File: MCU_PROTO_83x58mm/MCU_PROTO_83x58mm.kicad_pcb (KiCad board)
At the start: 2 copper layers, 75 x 49 mm, 251 parts, among them J1 Screw_Terminal_01x03, J10 Conn_01x01_Male, J2 Screw_Terminal_01x03, J3 Conn_01x20_Female, J4 Conn_01x20_Female, J5 Conn_01x20_Female, J6 Conn_01x20_Female, J7 Conn_01x20_Female, J8 Conn_01x20_Female, J9 Conn_01x01_Male

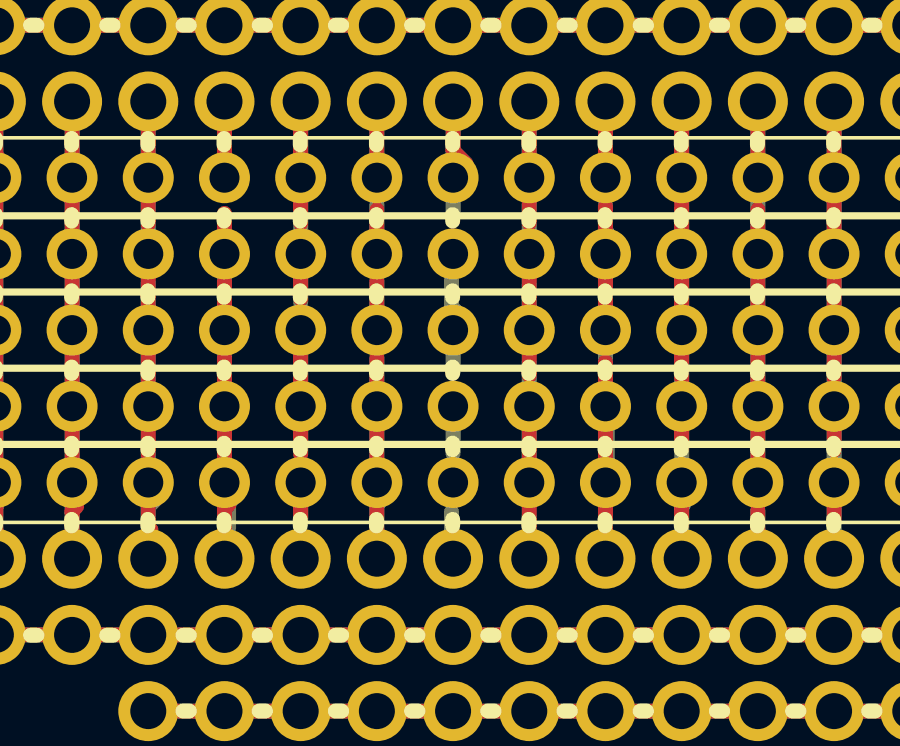
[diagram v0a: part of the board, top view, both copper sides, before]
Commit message: added missing trace
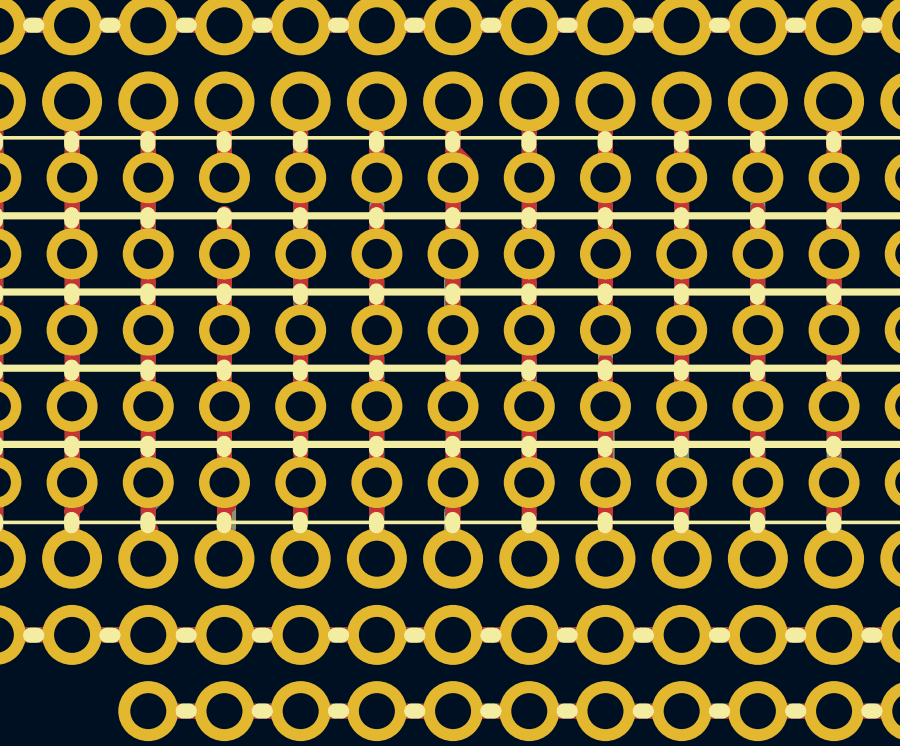
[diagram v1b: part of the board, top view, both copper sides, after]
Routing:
- net Net-(J8-Pad9): track 0.00 -> 4.41 mm
- net Net-(J7-Pad9): track 1.57 -> 4.44 mm
- net Net-(J6-Pad9): track 2.48 -> 4.79 mm
- net Net-(J5-Pad9): track 0.00 -> 2.21 mm
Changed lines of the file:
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@@
     (thickness 1.6)
     (drawings 284)
-    (tracks 720)
+    (tracks 728)
     (zones 0)
     (modules 251)
@@
   (segment (start 132.12 125.77) (end 132.12 124.1063) (width 0.5) (layer B.Cu) (net 74))
   (segment (start 132.12 125.77) (end 132.12 127.4718) (width 0.5) (layer F.Cu) (net 74))
+  (segment (start 129.58 125.77) (end 129.58 123.5564) (width 0.5) (layer F.Cu) (net 75))
   (segment (start 157.52 128.31) (end 157.52 126.7314) (width 0.5) (layer B.Cu) (net 76))
   (segment (start 157.52 128.31) (end 157.52 126.9092) (width 0.5) (layer F.Cu) (net 76))
@@
   (segment (start 129.5273 126.6317) (end 129.5273 127.5334) (width 0.5) (layer B.Cu) (net 87))
   (segment (start 129.58 128.31) (end 129.58 129.707) (width 0.5) (layer B.Cu) (net 87))
+  (segment (start 129.58 128.31) (end 129.58 125.9986) (width 0.5) (layer F.Cu) (net 87))
   (segment (start 157.52 130.85) (end 157.52 129.1444) (width 0.5) (layer B.Cu) (net 88))
   (segment (start 157.52 130.85) (end 157.52 128.7253) (width 0.5) (layer F.Cu) (net 88))
@@
   (segment (start 132.12 130.85) (end 132.12 132.6661) (width 0.5) (layer F.Cu) (net 98))
   (segment (start 129.58 130.85) (end 129.58 132.4248) (width 0.5) (layer B.Cu) (net 99))
+  (segment (start 129.58 130.85) (end 129.58 128.4751) (width 0.5) (layer F.Cu) (net 99))
+  (segment (start 129.58 128.4751) (end 129.3749 128.27) (width 0.5) (layer F.Cu) (net 99))
+  (segment (start 129.3749 126.3142) (end 129.5146 126.1745) (width 0.5) (layer F.Cu) (net 99))
   (segment (start 127.04 130.85) (end 127.04 129.3095) (width 0.5) (layer B.Cu) (net 100))
   (segment (start 127.04 130.85) (end 127.04 129.2117) (width 0.5) (layer F.Cu) (net 100))
@@
   (segment (start 132.12 133.39) (end 132.12 131.6463) (width 0.5) (layer B.Cu) (net 118))
   (segment (start 132.12 133.39) (end 132.12 134.9013) (width 0.5) (layer F.Cu) (net 118))
+  (segment (start 129.58 133.7202) (end 129.5146 133.6548) (width 0.5) (layer F.Cu) (net 119))
+  (segment (start 129.58 135.93) (end 129.58 133.7202) (width 0.5) (layer F.Cu) (net 119))
+  (segment (start 129.58 133.39) (end 129.58 131.278) (width 0.5) (layer F.Cu) (net 119))
   (segment (start 127.04 134.1355) (end 127.1143 134.0612) (width 0.5) (layer B.Cu) (net 120))
   (segment (start 127.04 135.93) (end 127.04 134.1355) (width 0.5) (layer B.Cu) (net 120))

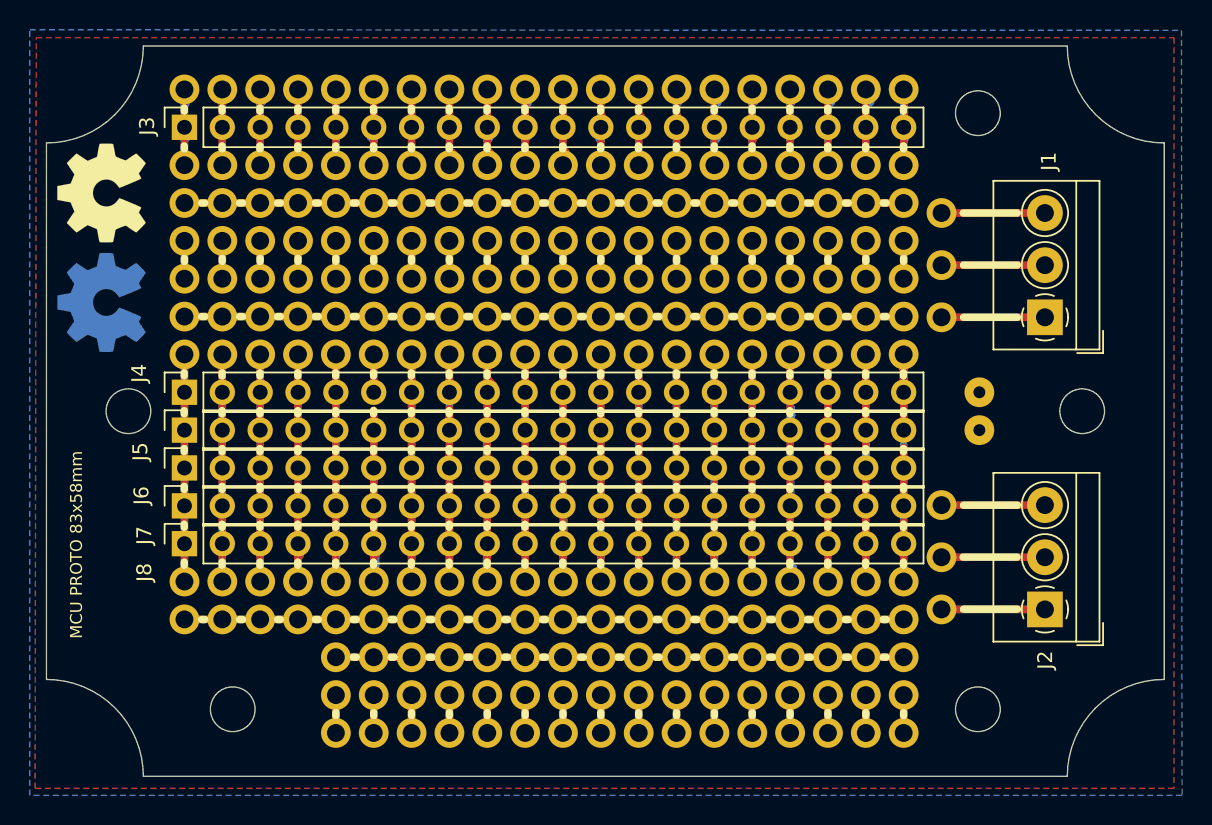
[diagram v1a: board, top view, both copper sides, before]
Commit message: added rpi zero compat started
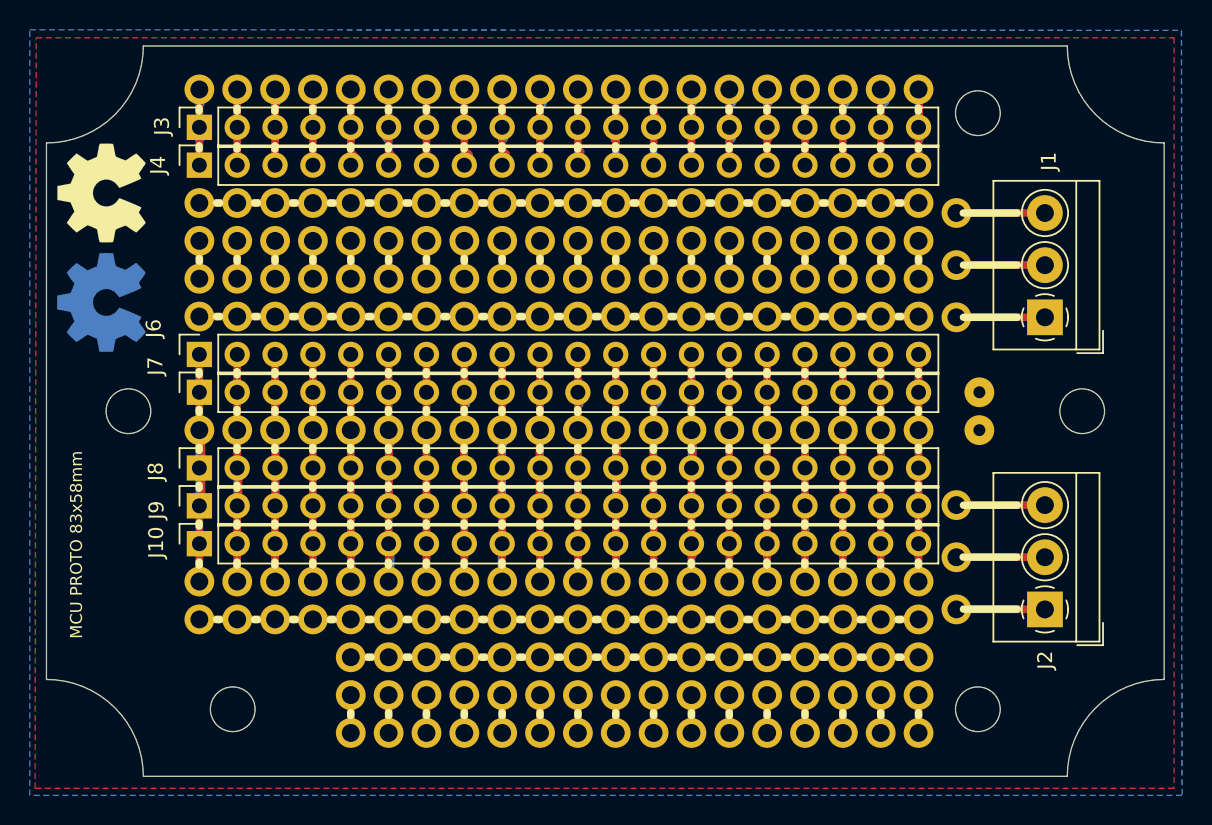
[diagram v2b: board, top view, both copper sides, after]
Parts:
- removed the REF** at (157.5, 108.0)
- removed the REF** at (155.0, 108.0)
- removed the REF** at (152.4, 108.0)
- removed the REF** at (149.9, 108.0)
- removed the REF** at (147.4, 108.0)
- removed the REF** at (144.8, 108.0)
- removed the REF** at (142.3, 108.0)
- removed the REF** at (139.7, 108.0)
- removed the REF** at (137.2, 108.0)
- removed the REF** at (134.7, 108.0)
- removed the REF** at (132.1, 108.0)
- removed the REF** at (129.6, 108.0)
- removed the REF** at (127.0, 108.0)
- removed the REF** at (124.5, 108.0)
- removed the REF** at (122.0, 108.0)
- removed the REF** at (119.4, 108.0)
- removed the REF** at (116.9, 108.0)
- removed the REF** at (114.3, 108.0)
- removed the REF** at (111.8, 108.0)
- removed the REF** at (109.3, 108.0)
- removed the REF** at (157.5, 120.7)
- removed the REF** at (155.0, 120.7)
- removed the REF** at (152.4, 120.7)
- removed the REF** at (149.9, 120.7)
- removed the REF** at (147.4, 120.7)
- removed the REF** at (144.8, 120.7)
- removed the REF** at (142.3, 120.7)
- removed the REF** at (139.7, 120.7)
- removed the REF** at (137.2, 120.7)
- removed the REF** at (134.7, 120.7)
- removed the REF** at (132.1, 120.7)
- removed the REF** at (129.6, 120.7)
- removed the REF** at (127.0, 120.7)
- removed the REF** at (124.5, 120.7)
- removed the REF** at (122.0, 120.7)
- removed the REF** at (119.4, 120.7)
- removed the REF** at (116.9, 120.7)
- removed the REF** at (114.3, 120.7)
- removed the REF** at (111.8, 120.7)
- removed the REF** at (109.3, 120.7)
- added J4: Conn_01x20_Female, Connector_PinSocket_2.54mm:PinSocket_1x20_P2.54mm_Vertical, F.Cu at (110.3, 108.0)
- added REF**: SolderWirePad_1x01_Drill0.8mm, Connector_Wire:SolderWirePad_1x01_Drill0.8mm, F.Cu at (158.5, 125.8)
- added REF**: SolderWirePad_1x01_Drill0.8mm, Connector_Wire:SolderWirePad_1x01_Drill0.8mm, F.Cu at (135.7, 125.8)
- added REF**: SolderWirePad_1x01_Drill0.8mm, Connector_Wire:SolderWirePad_1x01_Drill0.8mm, F.Cu at (133.1, 125.8)
- added REF**: SolderWirePad_1x01_Drill0.8mm, Connector_Wire:SolderWirePad_1x01_Drill0.8mm, F.Cu at (130.6, 125.8)
- added REF**: SolderWirePad_1x01_Drill0.8mm, Connector_Wire:SolderWirePad_1x01_Drill0.8mm, F.Cu at (128.0, 125.8)
- added REF**: SolderWirePad_1x01_Drill0.8mm, Connector_Wire:SolderWirePad_1x01_Drill0.8mm, F.Cu at (125.5, 125.8)
- added REF**: SolderWirePad_1x01_Drill0.8mm, Connector_Wire:SolderWirePad_1x01_Drill0.8mm, F.Cu at (123.0, 125.8)
- added REF**: SolderWirePad_1x01_Drill0.8mm, Connector_Wire:SolderWirePad_1x01_Drill0.8mm, F.Cu at (120.4, 125.8)
- added REF**: SolderWirePad_1x01_Drill0.8mm, Connector_Wire:SolderWirePad_1x01_Drill0.8mm, F.Cu at (117.9, 125.8)
- added REF**: SolderWirePad_1x01_Drill0.8mm, Connector_Wire:SolderWirePad_1x01_Drill0.8mm, F.Cu at (115.3, 125.8)
- added REF**: SolderWirePad_1x01_Drill0.8mm, Connector_Wire:SolderWirePad_1x01_Drill0.8mm, F.Cu at (112.8, 125.8)
- added REF**: SolderWirePad_1x01_Drill0.8mm, Connector_Wire:SolderWirePad_1x01_Drill0.8mm, F.Cu at (156.0, 125.8)
- added REF**: SolderWirePad_1x01_Drill0.8mm, Connector_Wire:SolderWirePad_1x01_Drill0.8mm, F.Cu at (110.3, 125.8)
- added REF**: SolderWirePad_1x01_Drill0.8mm, Connector_Wire:SolderWirePad_1x01_Drill0.8mm, F.Cu at (153.4, 125.8)
- added REF**: SolderWirePad_1x01_Drill0.8mm, Connector_Wire:SolderWirePad_1x01_Drill0.8mm, F.Cu at (150.9, 125.8)
- added REF**: SolderWirePad_1x01_Drill0.8mm, Connector_Wire:SolderWirePad_1x01_Drill0.8mm, F.Cu at (148.4, 125.8)
- added REF**: SolderWirePad_1x01_Drill0.8mm, Connector_Wire:SolderWirePad_1x01_Drill0.8mm, F.Cu at (145.8, 125.8)
- added REF**: SolderWirePad_1x01_Drill0.8mm, Connector_Wire:SolderWirePad_1x01_Drill0.8mm, F.Cu at (143.3, 125.8)
- added REF**: SolderWirePad_1x01_Drill0.8mm, Connector_Wire:SolderWirePad_1x01_Drill0.8mm, F.Cu at (140.7, 125.8)
- added REF**: SolderWirePad_1x01_Drill0.8mm, Connector_Wire:SolderWirePad_1x01_Drill0.8mm, F.Cu at (138.2, 125.8)
- moved J6 2.73 mm to (110.3, 120.7)
- moved J7 2.73 mm to (110.3, 123.2)
- moved J10 1.00 mm to (110.3, 133.4)
- moved J3 1.00 mm to (110.3, 105.5)
- moved J8 1.00 mm to (110.3, 128.3)
- moved J9 1.00 mm to (110.3, 130.8)
- moved REF** 1.00 mm to (140.7, 118.2)
- moved REF** 1.00 mm to (138.2, 118.2)
- moved REF** 1.00 mm to (135.7, 118.2)
- moved REF** 1.00 mm to (133.1, 118.2)
- moved REF** 1.00 mm to (130.6, 118.2)
- moved REF** 1.00 mm to (125.5, 118.2)
- moved REF** 1.00 mm to (123.0, 118.2)
- moved REF** 1.00 mm to (120.4, 118.2)
- moved REF** 1.00 mm to (117.9, 118.2)
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- renumbered J8 to J10, J9 to J11, J10 to J12, J4 to J6, J5 to J7, J6 to J8, J7 to J9
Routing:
- net Net-(J8-Pad1): track 3.90 -> 19.2 mm
- net Net-(J8-Pad2): track 4.21 -> 15.6 mm
- net Net-(J5-Pad1): track 0.00 -> 10.3 mm
- net Net-(J8-Pad8): track 3.21 -> 13.0 mm
- net Net-(J8-Pad3): track 3.25 -> 12.8 mm
- net Net-(J5-Pad2): track 0.00 -> 9.37 mm
- net Net-(J5-Pad3): track 0.00 -> 8.98 mm
- net Net-(J5-Pad14): track 0.00 -> 8.95 mm
- net Net-(J8-Pad6): track 3.42 -> 12.4 mm
- net Net-(J5-Pad6): track 0.00 -> 8.92 mm
- net Net-(J5-Pad16): track 0.00 -> 8.85 mm
- net Net-(J8-Pad11): track 3.67 -> 12.5 mm
- net Net-(J5-Pad9): track 0.00 -> 8.82 mm
- net Net-(J5-Pad8): track 0.00 -> 8.81 mm
- net Net-(J5-Pad18): track 0.00 -> 8.69 mm
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- added copper zone on B.Cu, net Net-(J10-Pad1)
- added copper zone on F.Cu, net Net-(J10-Pad1)
- removed copper zone on B.Cu, net Net-(J11-Pad1)
- removed copper zone on F.Cu, net Net-(J11-Pad1)

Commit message: pi zero added single gerber
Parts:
- removed the REF** at (158.5, 110.5)
- removed the REF** at (156.0, 110.5)
- removed the REF** at (153.4, 110.5)
- removed the REF** at (150.9, 110.5)
- removed the REF** at (148.4, 110.5)
- removed the REF** at (145.8, 110.5)
- removed the REF** at (143.3, 110.5)
- removed the REF** at (140.7, 110.5)
- removed the REF** at (138.2, 110.5)
- removed the REF** at (135.7, 110.5)
- removed the REF** at (133.1, 110.5)
- removed the REF** at (130.6, 110.5)
- removed the REF** at (128.0, 110.5)
- removed the REF** at (125.5, 110.5)
- removed the REF** at (123.0, 110.5)
- removed the REF** at (120.4, 110.5)
- removed the REF** at (117.9, 110.5)
- removed the REF** at (115.3, 110.5)
- removed the REF** at (112.8, 110.5)
- removed the REF** at (110.3, 110.5)
- added J5: Conn_01x20_Female, Connector_PinSocket_2.54mm:PinSocket_1x20_P2.54mm_Vertical, F.Cu at (110.3, 110.5)
- moved REF** 5.12 mm to (103.8, 115.0)
- moved J1 1.00 mm to (168.0, 118.2)
- moved J2 1.00 mm to (168.0, 137.8)
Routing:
- net (no net): track 579.8 -> 475.3 mm
- net Net-(J5-Pad2): track 9.37 -> 13.7 mm
- net Net-(J5-Pad19): track 7.09 -> 11.4 mm
- net Net-(J5-Pad16): track 8.85 -> 13.1 mm
- net Net-(J5-Pad6): track 8.92 -> 13.2 mm
- net Net-(J5-Pad15): track 6.80 -> 10.9 mm
- net Net-(J5-Pad20): track 8.67 -> 12.8 mm
- net Net-(J5-Pad13): track 8.67 -> 12.7 mm
- net Net-(J5-Pad9): track 8.82 -> 12.9 mm
- net Net-(J5-Pad4): track 7.60 -> 11.6 mm
- net Net-(J5-Pad3): track 8.98 -> 13.0 mm
- net Net-(J5-Pad17): track 7.00 -> 11.0 mm
- net Net-(J5-Pad10): track 6.51 -> 10.4 mm
- net Net-(J5-Pad5): track 6.15 -> 10.1 mm
- net Net-(J5-Pad12): track 6.48 -> 10.4 mm
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- added copper zone on B.Cu, net Net-(J11-Pad1)
- added copper zone on F.Cu, net Net-(J11-Pad1)
- removed copper zone on B.Cu, net Net-(J10-Pad1)
- removed copper zone on F.Cu, net Net-(J10-Pad1)

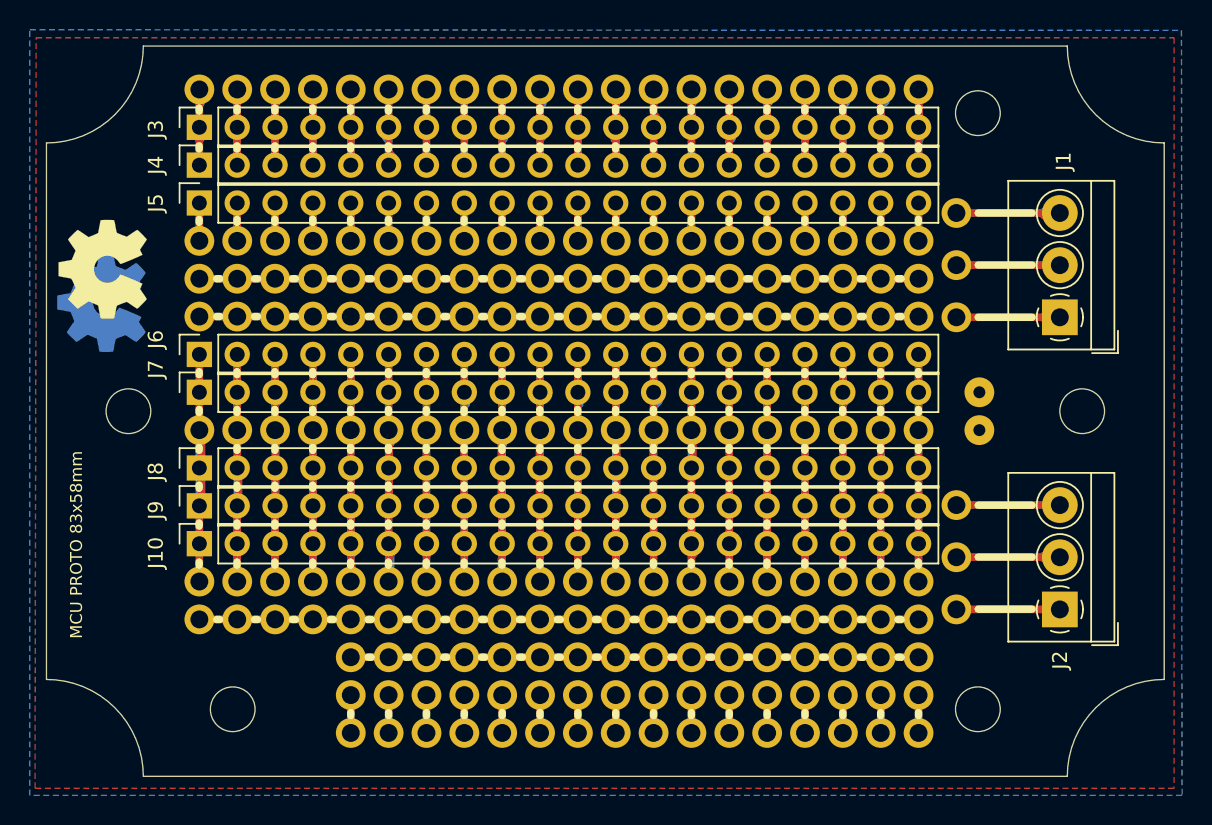
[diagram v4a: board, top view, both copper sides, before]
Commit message: +0.5mm shift
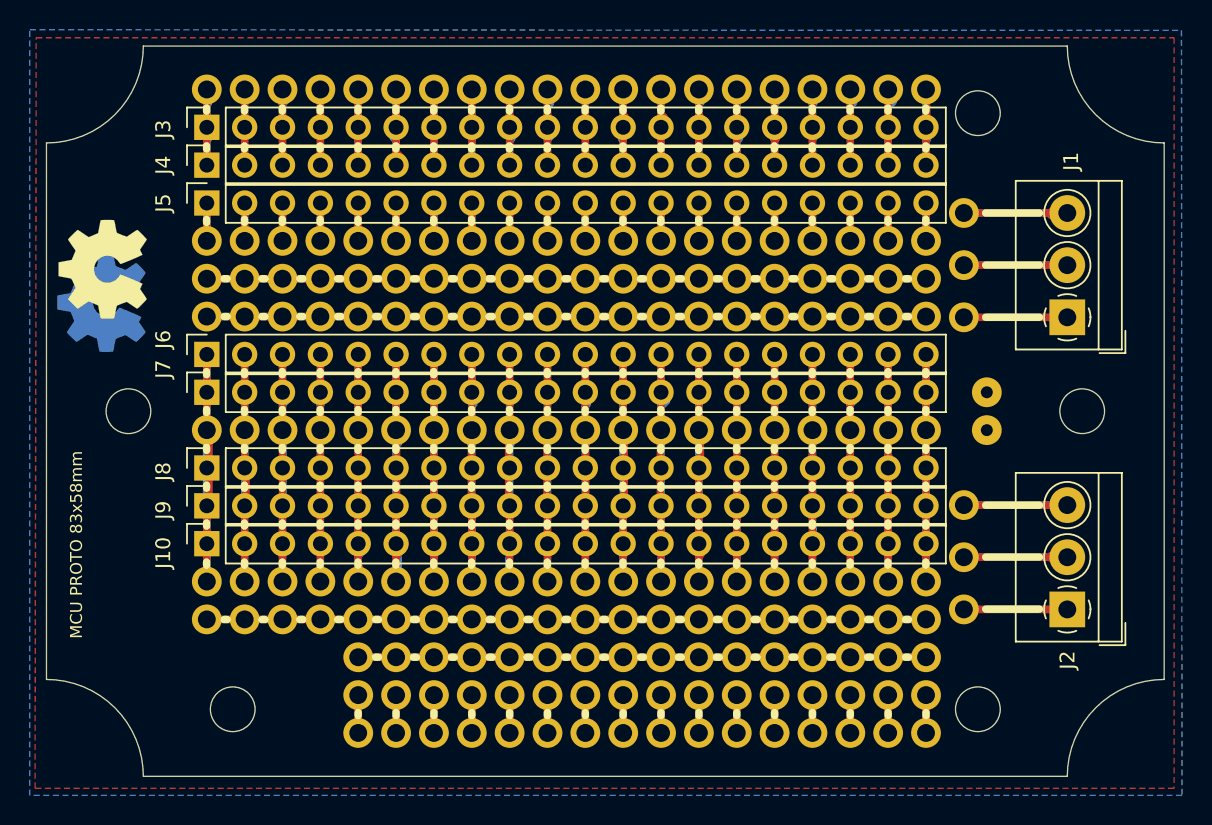
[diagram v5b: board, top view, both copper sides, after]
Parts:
- moved J1 0.50 mm to (168.5, 118.2)
- moved J10 0.50 mm to (110.8, 133.4)
- moved J11 0.50 mm to (163.1, 123.2)
- moved J12 0.50 mm to (163.1, 125.8)
- moved J2 0.50 mm to (168.5, 137.8)
- moved J3 0.50 mm to (110.8, 105.5)
- moved J4 0.50 mm to (110.8, 108.0)
- moved J5 0.50 mm to (110.8, 110.5)
- moved J6 0.50 mm to (110.8, 120.7)
- moved J7 0.50 mm to (110.8, 123.2)
- moved J8 0.50 mm to (110.8, 128.3)
- moved J9 0.50 mm to (110.8, 130.8)
- moved REF** 0.50 mm to (110.8, 113.1)
- moved REF** 0.50 mm to (138.7, 125.8)
- moved REF** 0.50 mm to (143.8, 118.2)
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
